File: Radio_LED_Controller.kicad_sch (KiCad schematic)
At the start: 13 parts, among them J1 Conn_01x04_Pin, J2 Conn_01x03_Pin, J3 Conn_01x05, J4 UPDI, J5 Conn_01x02_Pin, J6 Conn_01x02_Pin, J7 Conn_01x05, Q2 SS8050, Q3 SS8050, U1 ATtiny816-M

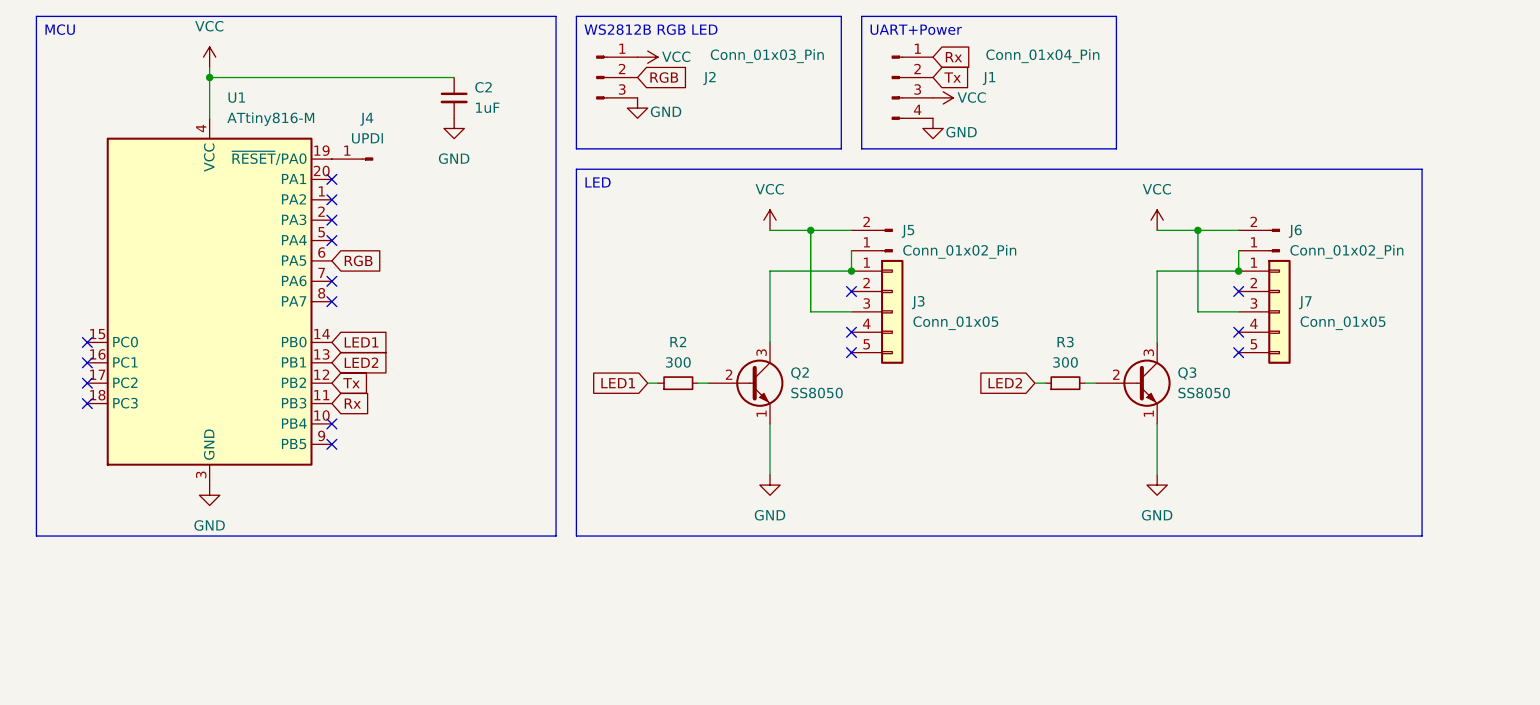
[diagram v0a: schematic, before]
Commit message: extra 2 RGB port
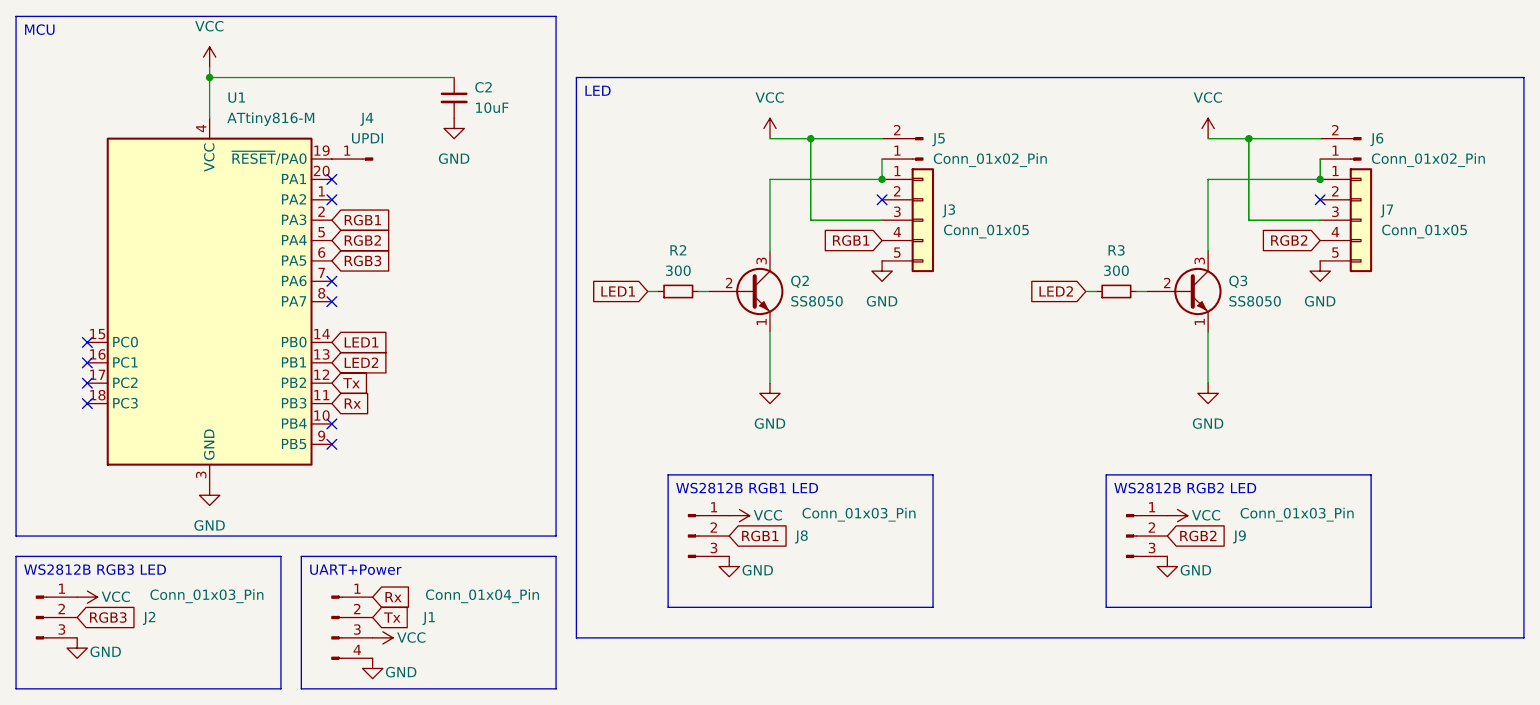
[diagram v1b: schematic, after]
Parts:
- added J8, J9: Conn_01x03_Pin, MyLib:SolderPad_01x03_1.5mm, symbol Connector:Conn_01x03_Pin
- C2: value 1uF -> 10uF
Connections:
- net GND: now also J3.5 (Pin_5), J7.5 (Pin_5), J8.3 (Pin_3), J9.3 (Pin_3)
- net VCC: now also J8.1 (Pin_1), J9.1 (Pin_1)
- net RGB1: now reaches U1.2 (PA3)
- net RGB1: now also J3.4 (Pin_4), J8.2 (Pin_2)
- net RGB2: now reaches U1.5 (PA4)
- net RGB2: now also J7.4 (Pin_4), J9.2 (Pin_2)
- net RGB renamed RGB3
- no-connect marks 18 -> 12
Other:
- moved on the sheet: J1, J2, J3, J5, J6, J7, Q2, Q3, R2, R3

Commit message: v0.2
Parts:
- J3, J7: footprint Connector_JST:JST_GH_SM05B-GHS-TB_1x05-1MP_P1.25mm_Horizontal -> Connector_Molex:Molex_PicoBlade_53261-0571_1x05-1MP_P1.25mm_Horizontal
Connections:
- net GND: now also J3.1 (Pin_1), J7.1 (Pin_1); no longer J3.5 (Pin_5), J7.5 (Pin_5)
- net LED1: now also U1.13 (PB1); no longer U1.14 (PB0)
- net LED2: now also U1.14 (PB0); no longer U1.13 (PB1)
- net RGB1: now also J3.2 (Pin_2), U1.6 (PA5); no longer J3.4 (Pin_4), U1.2 (PA3)
- net RGB2: now also J7.2 (Pin_2); no longer J7.4 (Pin_4)
- net RGB3: now also U1.2 (PA3); no longer U1.6 (PA5)
- net at J6.1 (Pin_1), Q3.3 (C): now also J7.5 (Pin_5); no longer J7.1 (Pin_1)
- net at J5.1 (Pin_1), Q2.3 (C): now also J3.5 (Pin_5); no longer J3.1 (Pin_1)
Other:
- moved on the sheet: J3, J5, J6, J7
